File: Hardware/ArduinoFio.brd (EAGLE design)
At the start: 27.9 x 64.8 mm, 43 parts, among them U1 MCP73831, U2 3.3V, U3 ATMEGA328, U4 XBEE-1B3, X1 USBSMD, Y1 8MHz

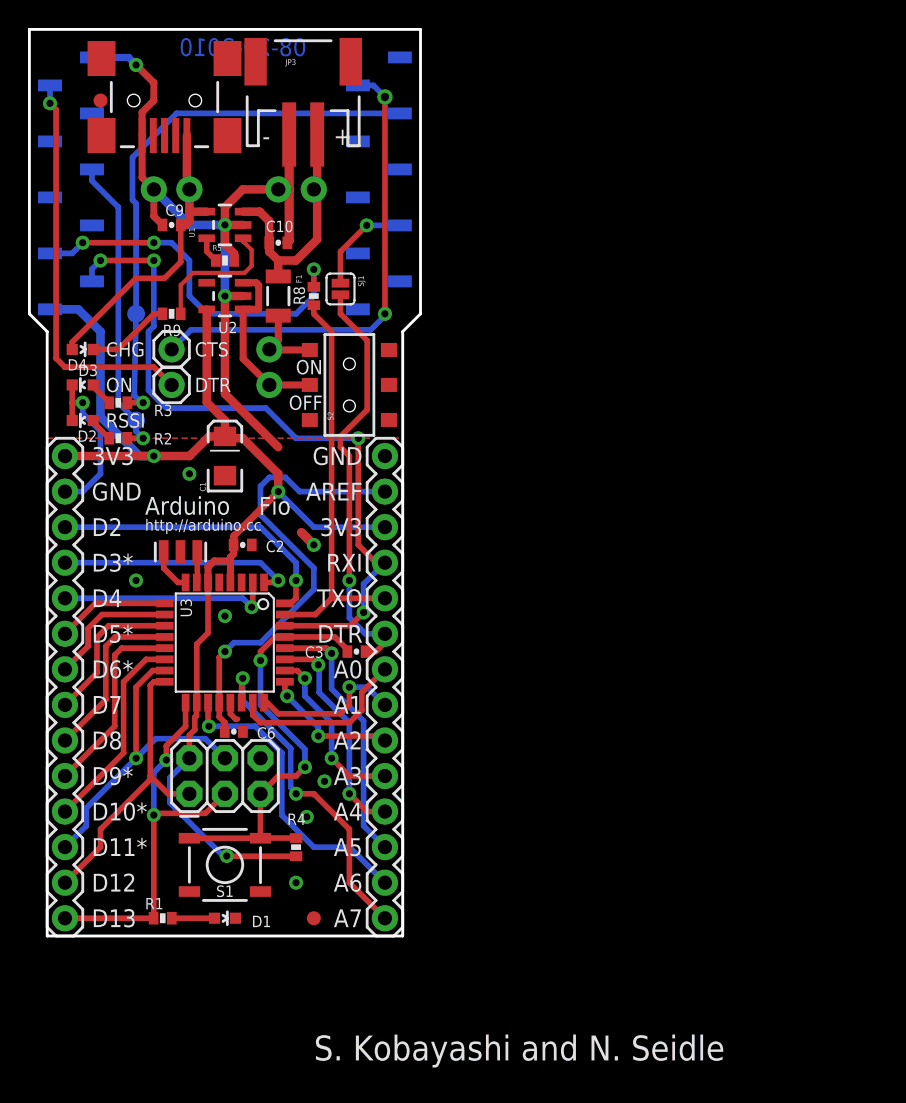
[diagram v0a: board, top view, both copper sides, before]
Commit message: added bottom side fiducials
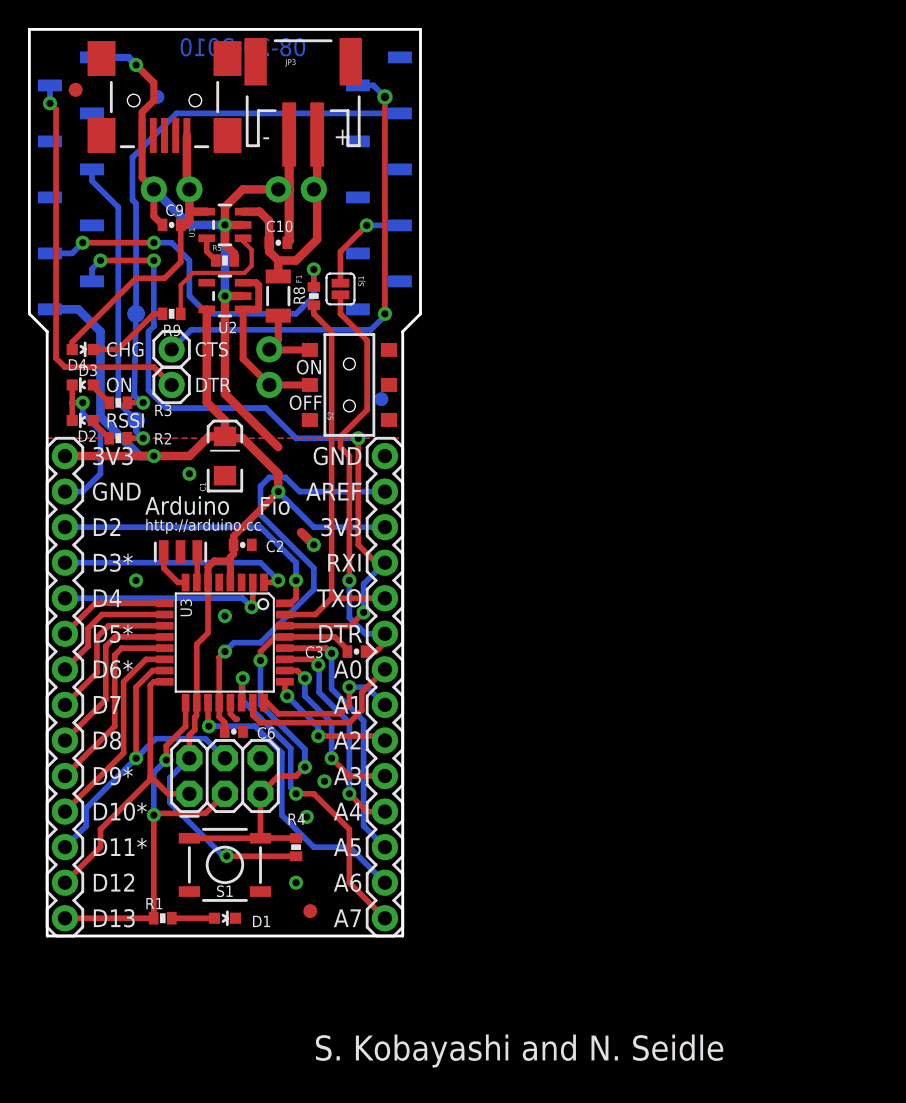
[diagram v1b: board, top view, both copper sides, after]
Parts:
- added FD1, FD2: FIDUCIAL1X2, SparkFun-Aesthetics:FIDUCIAL-1X2
- moved U$5 1.93 mm to (2.03, 60.5)
- moved U$4 0.57 mm to (18.8, 1.78)
